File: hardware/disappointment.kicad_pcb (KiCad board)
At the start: 2 copper layers, 197 x 75 mm, 56 parts, among them J1 Bus_ISA_16bit, J3 Conn_02x10_Odd_Even, J4 Conn_01x02, J5 ATX-24, U1 F85226AF

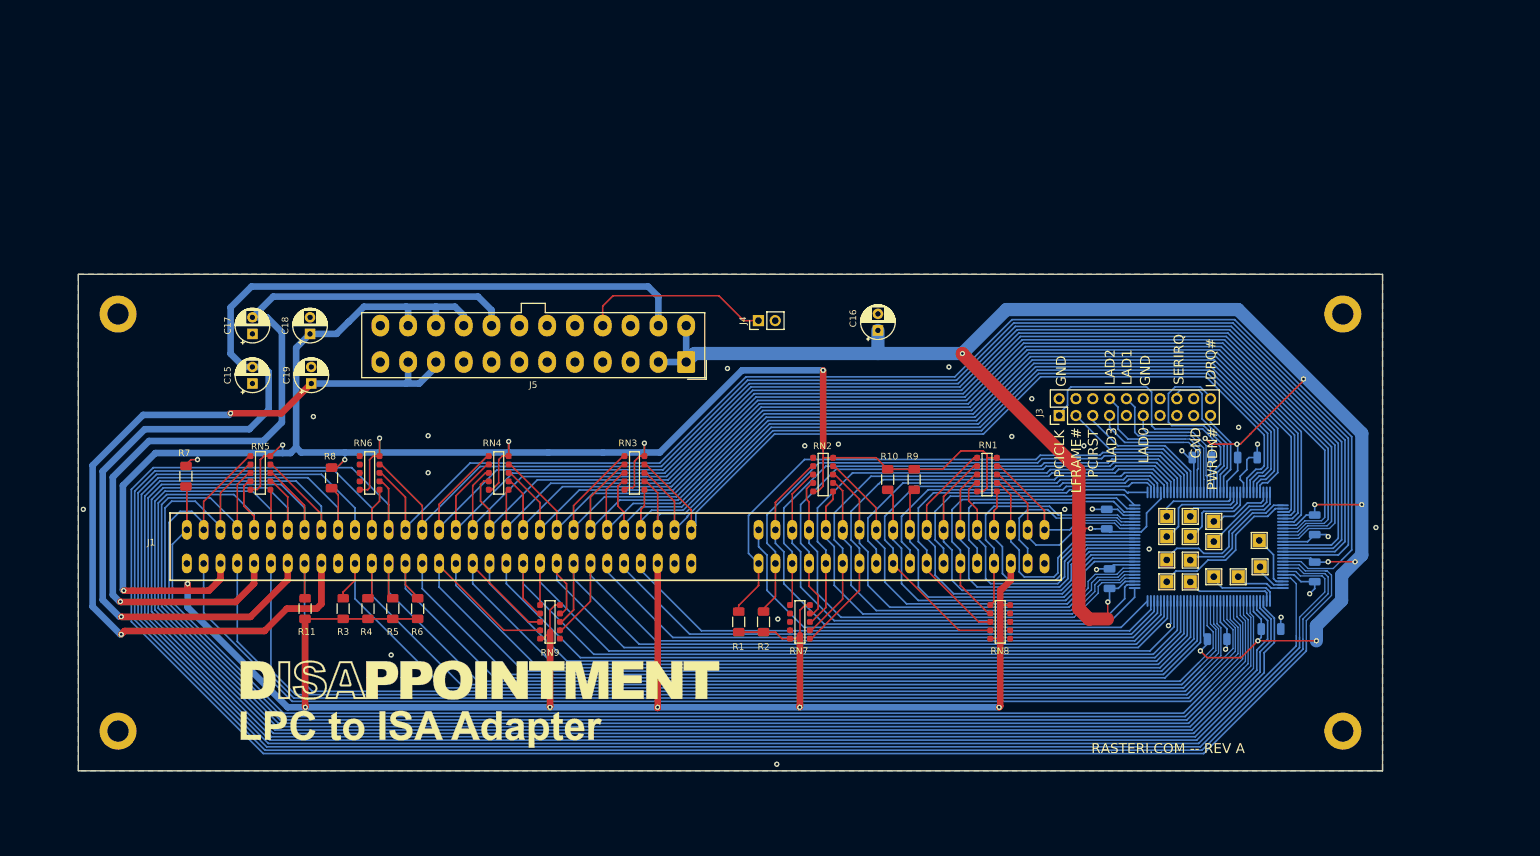
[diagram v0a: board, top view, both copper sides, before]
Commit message: started rerouting PCB
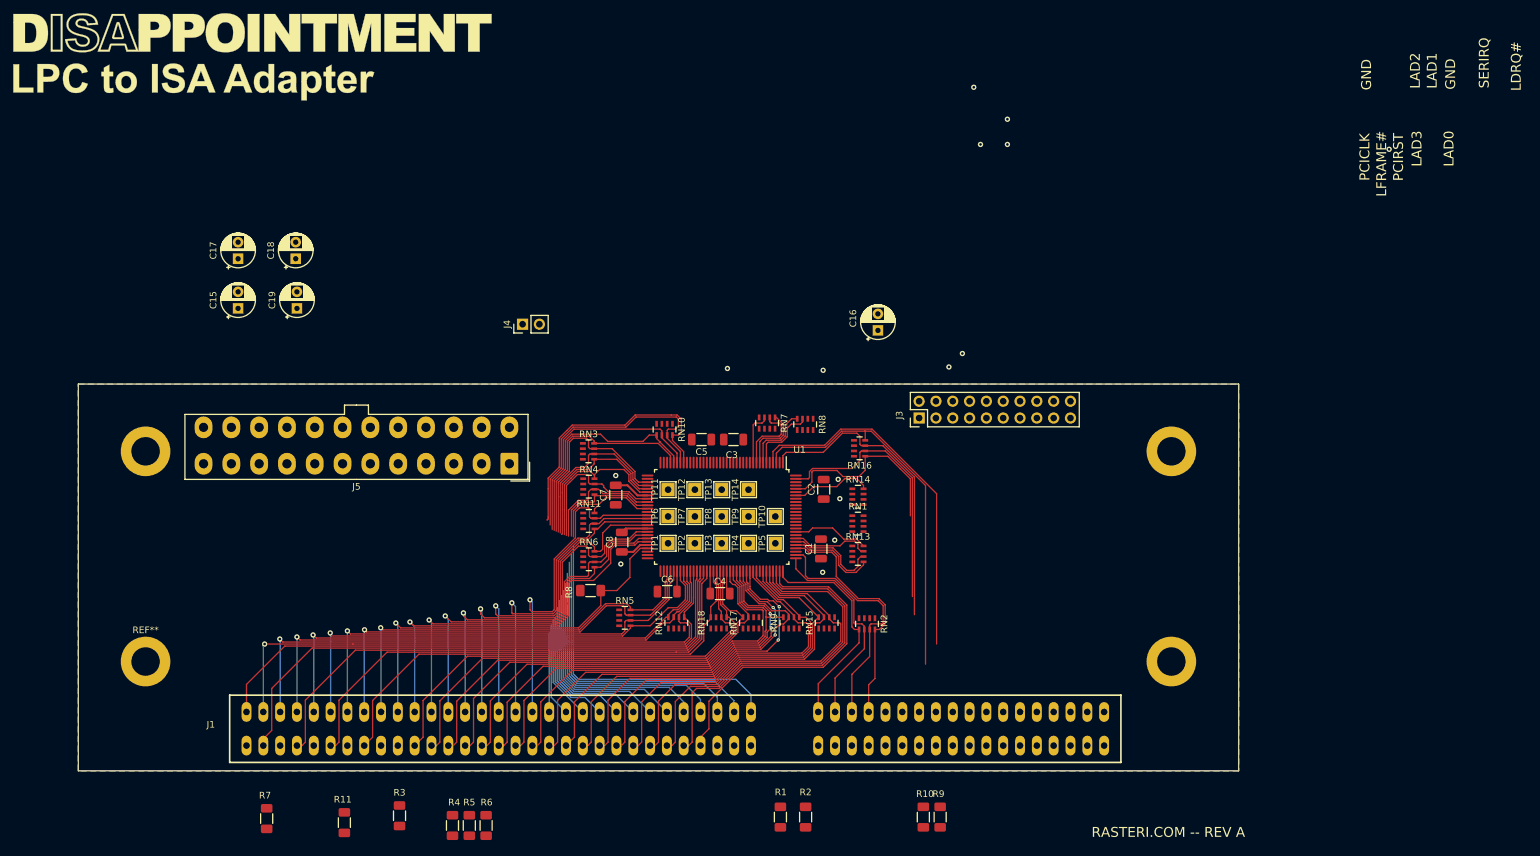
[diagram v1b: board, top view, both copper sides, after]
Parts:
- removed the ? at (250.0, 132.0)
- removed the ? at (250.0, 69.0)
- removed the ? at (65.0, 132.0)
- removed the REF** at (65.0, 69.0)
- added ?: , , F.Cu at (213.9, 89.7)
- added ?: , , F.Cu at (69.2, 89.7)
- added ?: , , F.Cu at (224.1, 121.5)
- added REF**: MountingHole_4.3mm_M4_DIN965_Pad, MountingHole:MountingHole_4.3mm_M4_DIN965_Pad, F.Cu at (69.2, 121.5)
- added RN10: 8.2K, Resistor_SMD:R_Array_Concave_4x0603, F.Cu at (147.5, 86.4)
- added RN11: 8.2K, Resistor_SMD:R_Array_Concave_4x0603, F.Cu at (136.1, 100.3)
- added RN12: 8.2K, Resistor_SMD:R_Array_Concave_4x0603, F.Cu at (149.3, 115.6)
- added RN13: 8.2K, Resistor_SMD:R_Array_Concave_4x0603, F.Cu at (176.8, 105.2)
- added RN14: 8.2K, Resistor_SMD:R_Array_Concave_4x0603, F.Cu at (176.8, 96.6)
- added RN15: 8.2K, Resistor_SMD:R_Array_Concave_4x0603, F.Cu at (172.0, 115.6)
- added RN16: 8.2K, Resistor_SMD:R_Array_Concave_4x0603, F.Cu at (177.0, 89.3)
- added RN17: 8.2K, Resistor_SMD:R_Array_Concave_4x0603, F.Cu at (160.6, 115.6)
- added RN18: 1K, Resistor_SMD:R_Array_Concave_4x0603, F.Cu at (155.7, 115.6)
- C1, C2, C3, C4, C5, C6, C7, C8, U1: moved to F.Cu
- R3, R4: value 1K -> 8.2K
- RN1, RN2, RN3, RN4, RN5, RN6, RN7, RN8, RN9: value R_Network08 -> 8.2K; footprint ps2usb:745C101 -> Resistor_SMD:R_Array_Concave_4x0603
- moved C7 105.7 mm to (140.2, 96.3)
- moved C8 104.8 mm to (141.1, 103.5)
- moved C6 91.4 mm to (148.0, 110.9), turned to 0 degrees
- moved TP11 90.2 mm to (148.1, 95.5), turned to 90 degrees
- moved TP12 85.6 mm to (152.1, 95.5), turned to 90 degrees
- moved C5 82.5 mm to (153.1, 88.0), turned to 180 degrees
- moved TP6 79.5 mm to (148.1, 99.6), turned to 90 degrees
- moved TP7 78.5 mm to (152.1, 99.6), turned to 90 degrees
- moved TP1 75.4 mm to (148.1, 103.6), turned to 90 degrees
- moved C4 75.4 mm to (155.9, 111.2), turned to 0 degrees
- moved TP8 74.9 mm to (156.2, 99.6), turned to 90 degrees
- moved U1 73.7 mm to (156.2, 99.6)
- moved TP2 71.3 mm to (152.1, 103.6), turned to 90 degrees
- moved TP3 70.9 mm to (156.2, 103.6), turned to 90 degrees
- moved C3 70.8 mm to (158.0, 88.0), turned to 0 degrees
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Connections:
- J5 pad 1: +3.3V -> Net-(F4-Pad1)
- J5 pad 10: +12V -> Net-(F1-Pad1)
- J5 pad 11: +12V -> Net-(F1-Pad1)
- J5 pad 12: +3.3V -> Net-(F4-Pad1)
- J5 pad 13: +3.3V -> Net-(F4-Pad1)
- J5 pad 14: -12V -> Net-(J5--12V)
- J5 pad 2: +3.3V -> Net-(F4-Pad1)
- J5 pad 20: -5V -> Net-(J5--5V)
- J5 pad 21: +5V -> Net-(F2-Pad1)
- J5 pad 22: +5V -> Net-(F2-Pad1)
- J5 pad 23: +5V -> Net-(F2-Pad1)
- J5 pad 4: +5V -> Net-(F2-Pad1)
- J5 pad 6: +5V -> Net-(F2-Pad1)
- R3 pad 1: +5V -> /DRQ2
- R3 pad 2: /SMEMW# -> GND
- R4 pad 1: +5V -> /IRQ9
- R4 pad 2: /SMEMR# -> +5V
- RN1 pad 2: /SD8 -> +5V
- RN1 pad 3: /SD9 -> +5V
- RN1 pad 4: /SD10 -> +5V
- RN1 pad 5: /SD11 -> /SD8
- RN1 pad 6: /SD12 -> /SD9
- RN1 pad 7: /SD13 -> /SD10
- RN1 pad 8: /SD14 -> /SD11
- RN2 pad 2: unconnected-(RN2-R1-Pad2) -> +5V
- RN2 pad 3: /LA23 -> +5V
- RN2 pad 4: /LA22 -> +5V
- RN2 pad 5: /LA21 -> /SBHE#
- RN2 pad 6: /LA20 -> /LA23
- RN2 pad 7: /LA19/GP23 -> /LA22
- RN2 pad 8: /LA18/GP22 -> /LA21
- RN3 pad 2: /SA7 -> +5V
- RN3 pad 3: /SA6 -> +5V
- RN3 pad 4: /SA5 -> +5V
- RN3 pad 5: /SA4 -> /SA7
- RN3 pad 6: /SA3 -> /SA6
- RN3 pad 7: /SA2 -> /SA5
- RN3 pad 8: /SA1 -> /SA4
- RN4 pad 2: /SA15 -> +5V
- RN4 pad 3: /SA14 -> +5V
- RN4 pad 4: /SA13 -> +5V
- RN4 pad 5: /SA12 -> /SA11
- RN4 pad 6: /SA11 -> /SA10
- RN4 pad 7: /SA10 -> /SA9
- RN4 pad 8: /SA9 -> /SA8
- RN5 pad 2: /SD7 -> +5V
- RN5 pad 3: /SD6 -> +5V
- RN5 pad 4: /SD5 -> +5V
- RN5 pad 5: /SD4 -> /SD3
- RN5 pad 6: /SD3 -> /SD2
- RN5 pad 7: /SD2 -> /SD1
- RN5 pad 8: /SD1 -> /SD0
- RN6 pad 2: unconnected-(RN6-R1-Pad2) -> +5V
- RN6 pad 3: unconnected-(RN6-R2-Pad3) -> +5V
- RN6 pad 4: unconnected-(RN6-R3-Pad4) -> +5V
- RN6 pad 5: unconnected-(RN6-R4-Pad5) -> /SA19
- RN6 pad 6: /SA19 -> /SA18
- RN6 pad 7: /SA18 -> /SA17
- RN6 pad 8: /SA17 -> /SA16
- RN7 pad 1: +5V -> /IRQ12
- RN7 pad 2: /IRQ14 -> /IRQ11
- RN7 pad 3: /IRQ15 -> /IRQ10
- RN7 pad 4: /IRQ12 -> unconnected-(RN7-R4.1-Pad4)
- RN7 pad 5: /IRQ11 -> +5V
- RN7 pad 6: /IRQ10 -> +5V
- RN7 pad 7: unconnected-(RN7-R6-Pad7) -> +5V
- RN7 pad 8: unconnected-(RN7-R7-Pad8) -> +5V
- RN8 pad 1: +5V -> unconnected-(RN8-R1.1-Pad1)
- RN8 pad 3: unconnected-(RN8-R2-Pad3) -> /IRQ14
- RN8 pad 4: unconnected-(RN8-R3-Pad4) -> /IRQ15
- RN8 pad 5: unconnected-(RN8-R4-Pad5) -> +5V
- RN8 pad 6: /DRQ7 -> +5V
- RN8 pad 7: /DRQ6 -> +5V
- RN8 pad 8: /DRQ5 -> +5V
- RN9 pad 2: unconnected-(RN9-R1-Pad2) -> +5V
- RN9 pad 3: /IRQ3 -> +5V
- RN9 pad 4: /IRQ4 -> +5V
- RN9 pad 5: /IRQ5 -> /IRQ6
- RN9 pad 6: /IRQ6 -> /IRQ7
- RN9 pad 7: /IRQ7 -> /DRQ1
- RN9 pad 8: /DRQ1 -> /DRQ3
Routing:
- net +5V: track 562.8 -> 0.00 mm, vias 14 -> 1
- net +3.3V: track 332.2 -> 16.6 mm, vias 13 -> 7
- net /SA18: track 287.7 -> 55.3 mm, vias 0 -> 1
- net /SA19: track 279.5 -> 57.2 mm, vias 0 -> 1
- net /AEN: track 266.7 -> 59.5 mm, vias 0 -> 1
- net /IOCHRDY: track 261.3 -> 60.1 mm, vias 0 -> 1
- net /SD0: track 257.2 -> 63.0 mm, vias 0 -> 1
- net /SD1: track 249.4 -> 66.4 mm, vias 0 -> 1
- net /SD2: track 241.7 -> 68.5 mm, vias 0 -> 1
- net -12V: track 172.7 -> 0.00 mm, vias 1 -> 0
- net /SD3: track 232.6 -> 73.1 mm, vias 0 -> 1
- net /SD4: track 229.3 -> 75.6 mm, vias 0 -> 1
- net /SA17: track 203.1 -> 56.4 mm, vias 0 -> 1
- net /SA12: track 176.2 -> 30.2 mm
- net /SD5: track 224.2 -> 78.3 mm, vias 0 -> 1
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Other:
- board size 197 x 75 mm -> 175.3 x 58.4 mm

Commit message: getting there
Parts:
- added F1: Polyfuse, Fuse:Fuse_1206_3216Metric, F.Cu at (93.0, 102.7)
- added F2: Polyfuse, Fuse:Fuse_1206_3216Metric, F.Cu at (113.4, 102.9)
- added F4: Polyfuse, Fuse:Fuse_1206_3216Metric, F.Cu at (128.1, 84.4)
- added F5: Polyfuse, Fuse:Fuse_1206_3216Metric, F.Cu at (94.0, 85.0)
- added F6: Polyfuse, Fuse:Fuse_1206_3216Metric, F.Cu at (117.3, 82.4)
- moved RN7 54.0 mm to (209.4, 113.2), turned to 0 degrees
- moved RN8 51.2 mm to (209.4, 116.9), turned to 0 degrees
- moved C16 48.5 mm to (133.0, 84.4)
- moved C18 46.5 mm to (108.3, 104.1)
- moved RN16 45.1 mm to (209.4, 120.7), turned to 0 degrees
- moved C17 40.9 mm to (86.8, 101.4), turned to -90 degrees
- moved C19 36.2 mm to (97.4, 103.9)
- moved C15 34.2 mm to (74.8, 101.4), turned to -90 degrees
- moved R1 33.7 mm to (188.2, 120.5)
- moved R4 30.5 mm to (95.8, 123.0), turned to 90 degrees
- moved TP1 29.7 mm to (146.9, 73.9)
- moved TP11 29.7 mm to (146.9, 65.8)
- moved TP12 29.7 mm to (151.0, 65.8)
- moved TP13 29.7 mm to (155.0, 65.8)
- moved TP14 29.7 mm to (159.1, 65.8)
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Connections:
- RN16 pad 1: /DRQ7 -> /DRQ0
- RN16 pad 2: /DRQ6 -> /DRQ5
- RN16 pad 3: /DRQ5 -> /DRQ6
- RN16 pad 4: /DRQ0 -> /DRQ7
- RN7 pad 1: /IRQ12 -> unconnected-(RN7-R1.1-Pad1)
- RN7 pad 2: /IRQ11 -> /IRQ10
- RN7 pad 3: /IRQ10 -> /IRQ11
- RN7 pad 4: unconnected-(RN7-R4.1-Pad4) -> /IRQ12
- RN8 pad 1: unconnected-(RN8-R1.1-Pad1) -> /IRQ15
- RN8 pad 2: unconnected-(RN8-R2.1-Pad2) -> /IRQ14
- RN8 pad 3: /IRQ14 -> unconnected-(RN8-R3.1-Pad3)
- RN8 pad 4: /IRQ15 -> unconnected-(RN8-R4.1-Pad4)
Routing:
- net +5V: track 0.00 -> 475.9 mm, vias 1 -> 24
- net -12V: track 0.00 -> 117.4 mm, vias 0 -> 1
- net /MEMCS16#: track 0.00 -> 113.9 mm, vias 0 -> 2
- net /IOCS16#: track 0.00 -> 108.9 mm, vias 0 -> 2
- net /IRQ10: track 8.16 -> 109.4 mm, vias 0 -> 1
- net /IRQ11: track 11.3 -> 105.1 mm, vias 0 -> 1
- net /IRQ12: track 10.4 -> 103.3 mm, vias 0 -> 1
- net /IRQ15: track 10.6 -> 99.6 mm, vias 0 -> 1
- net /IRQ14: track 10.9 -> 97.5 mm, vias 0 -> 1
- net /DACK5#: track 0.00 -> 83.7 mm, vias 0 -> 1
- net /SERIRQ: track 0.00 -> 79.3 mm
- net /PWRDN#: track 0.00 -> 78.2 mm
- net /DACK6#/HEFRAS: track 0.00 -> 77.0 mm, vias 0 -> 1
- net +3.3V: track 16.6 -> 93.2 mm, vias 7 -> 8
- net -5V: track 0.00 -> 75.0 mm, vias 0 -> 1
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- added copper zone on F.Cu, net +3.3V

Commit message: getting there more
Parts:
- removed R11: 1K, Resistor_SMD:R_1206_3216Metric_Pad1.30x1.75mm_HandSolder
- removed R5, R6: 8.2K, Resistor_SMD:R_1206_3216Metric_Pad1.30x1.75mm_HandSolder
- moved RN12 58.5 mm to (90.8, 114.4), turned to -90 degrees
- moved R2 53.8 mm to (238.9, 122.2)
- moved R9 53.8 mm to (248.2, 122.2)
- moved R1 53.8 mm to (242.0, 122.2)
- moved R10 53.8 mm to (245.0, 122.2)
- moved RN18 48.9 mm to (107.6, 123.9), turned to -90 degrees
- moved RN17 43.5 mm to (117.8, 123.1)
- moved RN5 39.6 mm to (101.9, 114.5), turned to -90 degrees
- moved C2 25.7 mm to (197.0, 98.7)
- moved C5 25.7 mm to (177.1, 91.2)
- moved C6 25.7 mm to (173.4, 114.1)
- moved U1 25.7 mm to (181.6, 102.9)
- moved C1 25.7 mm to (196.6, 107.7)
- moved C3 25.7 mm to (183.4, 91.2)
- moved C7 25.7 mm to (167.3, 100.7)
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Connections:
- RN18 pad 5: /SMEMR# -> /OWS#
- RN18 pad 6: /SMEMW# -> unconnected-(RN18-R3.2-Pad6)
- RN18 pad 7: unconnected-(RN18-R2.2-Pad7) -> /SMEMW#
- RN18 pad 8: /OWS# -> /SMEMR#
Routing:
- net +5V: track 475.9 -> 392.4 mm, vias 24 -> 14
- net /SERIRQ: track 79.3 -> 23.1 mm, vias 0 -> 1
- net /PWRDN#: track 78.2 -> 25.5 mm, vias 0 -> 1
- net /LAD0: track 55.6 -> 14.4 mm, vias 0 -> 1
- net /SA0: track 96.3 -> 55.3 mm
- net /SA1: track 94.7 -> 54.1 mm
- net /LAD1: track 51.5 -> 13.2 mm
- net /LAD3: track 46.9 -> 10.8 mm, vias 0 -> 1
- net /LDRQ#: track 67.4 -> 31.7 mm, vias 0 -> 2
- net /PCICLK: track 47.0 -> 14.0 mm, vias 1 -> 0
- net /LAD2: track 49.0 -> 19.5 mm
- net /SA2: track 83.6 -> 56.4 mm
- net /SD3: track 73.1 -> 100.2 mm
- net /PCIRST#: track 44.0 -> 17.1 mm, vias 0 -> 1
- net /SD4: track 75.6 -> 102.5 mm
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
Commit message: about done
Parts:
- removed J4: Conn_01x02, Connector_PinHeader_2.54mm:PinHeader_1x02_P2.54mm_Vertical
- removed TP1, TP10, TP11, TP12, TP13, TP14, TP2, TP3, TP4, TP5, TP6, TP7, TP8, TP9: TestPoint, TestPoint:TestPoint_THTPad_2.0x2.0mm_Drill1.0mm
- added ?: , , F.Cu at (69.2, 131.7)
- added ?: , , F.Cu at (224.1, 131.7)
- added R5: 10K, Resistor_SMD:R_1206_3216Metric_Pad1.30x1.75mm_HandSolder, F.Cu at (166.3, 93.5)
- added R6: DNP, Resistor_SMD:R_1206_3216Metric_Pad1.30x1.75mm_HandSolder, F.Cu at (215.1, 115.6)
- moved F6 50.7 mm to (69.9, 100.4), turned to -90 degrees
- moved R9 45.8 mm to (202.4, 122.0)
- moved R10 45.6 mm to (199.5, 122.0)
- moved R1 28.9 mm to (224.8, 99.0), turned to 180 degrees
- moved R2 24.5 mm to (224.8, 102.2), turned to 180 degrees
- moved F5 22.8 mm to (76.9, 100.1), turned to -90 degrees
- moved C16 12.3 mm to (145.3, 86.0)
- moved F4 10.5 mm to (138.5, 86.0)
- moved RN12 9.83 mm to (99.6, 110.1)
- moved C15 9.10 mm to (67.7, 107.0), turned to 0 degrees
- moved C17 8.66 mm to (80.3, 107.0), turned to 180 degrees
- moved RN5 4.87 mm to (104.0, 110.0)
- moved J5 4.58 mm to (127.6, 91.3)
- moved RN10 3.48 mm to (169.0, 88.7), turned to 0 degrees
- moved C19 3.32 mm to (97.4, 100.6)
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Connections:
- J5 pad 16: Net-(J4-Pin_1) -> unconnected-(J5-PS_ON#-Pad16)
- RN18 pad 1: +5V -> /SMEMR#
- RN18 pad 2: +5V -> /SMEMW#
- RN18 pad 3: +5V -> unconnected-(RN18-R3.1-Pad3)
- RN18 pad 4: +5V -> /OWS#
- RN18 pad 5: /OWS# -> +5V
- RN18 pad 6: unconnected-(RN18-R3.2-Pad6) -> +5V
- RN18 pad 7: /SMEMW# -> +5V
- RN18 pad 8: /SMEMR# -> +5V
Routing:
- net +5V: track 392.4 -> 572.4 mm, vias 14 -> 19
- net +3.3V: track 75.0 -> 165.7 mm, vias 7 -> 9
- net Net-(J5--12V): track 8.83 -> 71.0 mm
- net -12V: track 116.2 -> 56.6 mm
- net Net-(J5--5V): track 5.54 -> 37.3 mm
- net -5V: track 77.4 -> 50.5 mm
- net /SA8: track 62.7 -> 86.8 mm
- net /SA9: track 65.5 -> 87.9 mm
- net /SA10: track 65.1 -> 81.9 mm
- net /SA11: track 67.0 -> 80.5 mm
- net /SA0: track 55.3 -> 66.6 mm
- net /SA2: track 56.4 -> 67.0 mm
- net /SA12: track 69.0 -> 79.6 mm
- net /IOCS16#: track 95.5 -> 106.0 mm
- net /MEMCS16#: track 101.2 -> 111.1 mm
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- added copper zone on B.Cu, net +3.3V
- removed copper zone on F.Cu, net +3.3V
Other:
- board text added: "RASTERI.COM -- REV B"
- board text removed: "GND"
- board text removed: "LAD0"
- board text removed: "LAD1"
- board text removed: "LAD2"
- board text removed: "LAD3"
- board text removed: "LDRQ#"
- board text removed: "LFRAME#"
- board text removed: "PCICLK"
- board text removed: "PCIRST"
- board text removed: "PWRDN#"
- board text removed: "RASTERI.COM -- REV A"
- board text removed: "SERIRQ"
